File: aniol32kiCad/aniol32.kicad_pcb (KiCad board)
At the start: 2 copper layers, 55 parts, among them J1 RST, J2 PWR, J5 Buzzer, U1 74LS32, U10 74LS590, U11 74LS573, U12 74LS74, U13 74LS151, U14 74LS138, U2 74LS14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

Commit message: added bitmapped text bin file generator
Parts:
- removed U8: KM62256CLP, Package_DIP:DIP-28_W15.24mm_Socket
- CPU1: renamed from U6; value Z80CPU -> Z80
- D1: footprint Diode_THT:D_A-405_P7.62mm_Horizontal -> Diode_THT:D_5KPW_P7.62mm_Vertical_AnodeUp
- R11, R13: value 1k -> 4k7
- SERIAL1: value Conn_02x08_Counter_Clockwise -> Conn_02x08
- U9: value DART-DIP-40 -> DART
- moved R1 75.3 mm to (246.8, 135.0)
- moved R4 75.3 mm to (226.7, 124.7)
- moved R6 75.3 mm to (230.7, 114.4)
- moved R8 75.3 mm to (230.7, 118.5)
- moved RV1 75.3 mm to (219.4, 147.0)
- moved R2 75.3 mm to (247.4, 141.5)
- moved R5 75.3 mm to (215.9, 128.7)
- moved R7 75.3 mm to (215.9, 124.7)
- moved C3 66.4 mm to (125.1, 39.1), turned to 0 degrees
- moved ROM1 54.7 mm to (106.4, 46.6)
- moved U1 51.5 mm to (138.4, 101.1)
- moved C10 50.9 mm to (135.1, 99.6)
- moved J5 36.1 mm to (152.4, 38.9)
- moved C13 32.9 mm to (80.6, 57.5)
- moved U13 32.9 mm to (83.9, 58.7)
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- renumbered U7 to ROM1
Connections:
- CPU1 pad 17: Net-(R11-Pad1) -> NMI
- CPU1 pad 24: Net-(R13-Pad1) -> WAIT
- CPU1 pad 29: (no net) -> GND
- CPU1 pad 5: A15 -> (no net)
- R11 pad 1: Net-(R11-Pad1) -> NMI
- R13 pad 1: Net-(R13-Pad1) -> WAIT
- ROM1 pad 20: ROMSEL -> MEMRQ
- SERIAL1 pad 11: (no net) -> Net-(SERIAL1-Pad11)
- SERIAL1 pad 13: (no net) -> Net-(SERIAL1-Pad13)
- SERIAL1 pad 14: (no net) -> Net-(SERIAL1-Pad14)
- SERIAL1 pad 15: (no net) -> Net-(SERIAL1-Pad15)
- SERIAL1 pad 16: +5V -> GND
- SERIAL1 pad 7: Net-(SERIAL1-Pad7) -> CLK
- SERIAL1 pad 8: GND -> +5V
- SERIAL1 pad 9: CLK -> Net-(SERIAL1-Pad9)
- U1 pad 1: A15 -> (no net)
- U1 pad 2: MEMRQ -> (no net)
- U1 pad 3: RAMSEL -> (no net)
- U1 pad 4: MEMRQ -> (no net)
- U1 pad 5: Net-(U1-Pad5) -> (no net)
- U1 pad 6: ROMSEL -> (no net)
- U2 pad 1: A15 -> (no net)
- U2 pad 2: Net-(U1-Pad5) -> (no net)
- U9 pad 11: (no net) -> Net-(SERIAL1-Pad6)
- U9 pad 12: (no net) -> Net-(SERIAL1-Pad2)
- U9 pad 13: (no net) -> Net-(SERIAL1-Pad3)
- U9 pad 14: (no net) -> Net-(SERIAL1-Pad5)
- U9 pad 15: (no net) -> Net-(SERIAL1-Pad4)
- U9 pad 22: Net-(SERIAL1-Pad10) -> Net-(SERIAL1-Pad1)
- U9 pad 23: Net-(SERIAL1-Pad6) -> Net-(SERIAL1-Pad14)
- U9 pad 24: Net-(SERIAL1-Pad5) -> Net-(SERIAL1-Pad13)
- U9 pad 25: Net-(SERIAL1-Pad7) -> Net-(SERIAL1-Pad15)
- U9 pad 26: Net-(SERIAL1-Pad2) -> Net-(SERIAL1-Pad10)
- U9 pad 28: Net-(SERIAL1-Pad1) -> Net-(SERIAL1-Pad9)
- U9 pad 29: Net-(SERIAL1-Pad3) -> Net-(SERIAL1-Pad11)
- U9 pad 30: Net-(SERIAL1-Pad4) -> WAIT

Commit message: working on the calculator and the A32 pcb
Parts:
- D1: footprint Diode_THT:D_5KPW_P7.62mm_Vertical_AnodeUp -> Diode_THT:D_DO-15_P2.54mm_Vertical_AnodeUp
- RV1: footprint Potentiometer_THT:Potentiometer_TT_P0915N -> Potentiometer_THT:Potentiometer_Vishay_T73XW_Horizontal
- moved R2 251.9 mm to (14.6, 45.2)
- moved R1 201.7 mm to (72.5, 33.4), turned to 180 degrees
- moved RV1 186.9 mm to (85.9, 16.3), turned to 90 degrees
- moved R8 155.2 mm to (89.7, 53.6), turned to 90 degrees
- moved R6 147.5 mm to (96.3, 53.6), turned to 90 degrees
- moved R7 142.0 mm to (93.0, 53.6), turned to 90 degrees
- moved R5 138.5 mm to (99.6, 53.6), turned to 90 degrees
- moved R4 81.2 mm to (148.5, 102.7), turned to 90 degrees
- moved C7 40.4 mm to (110.2, 44.4)
- moved U3 40.4 mm to (113.5, 45.6)
- moved ROM1 34.0 mm to (140.3, 49.4)
- moved C3 34.0 mm to (159.0, 41.9)
- moved J5 25.3 mm to (172.3, 23.2)
- moved U4 23.9 mm to (158.4, 84.8)
- moved C2 23.3 mm to (154.9, 83.1)
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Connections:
- U12 pad 13: GND -> +5V

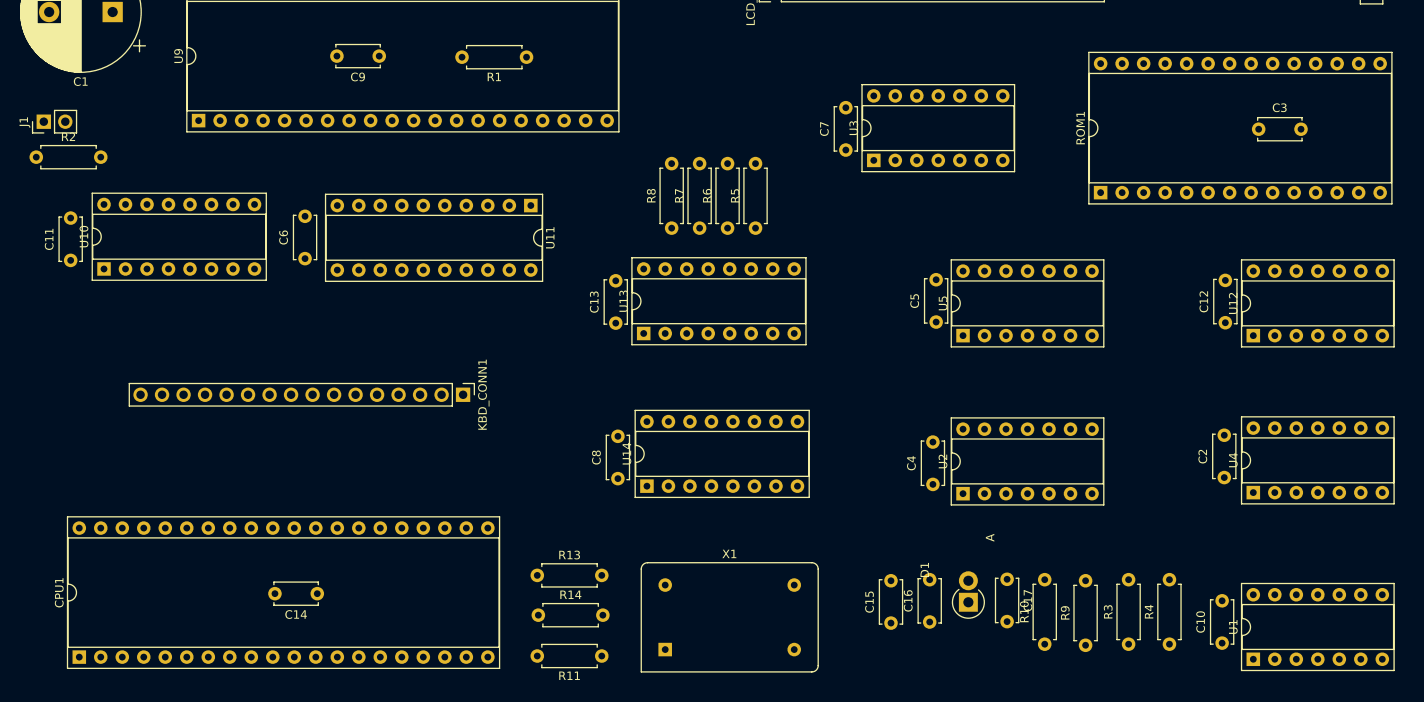
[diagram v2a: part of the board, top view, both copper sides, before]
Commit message: New A32 PCB layout
With CPU closer to the memory
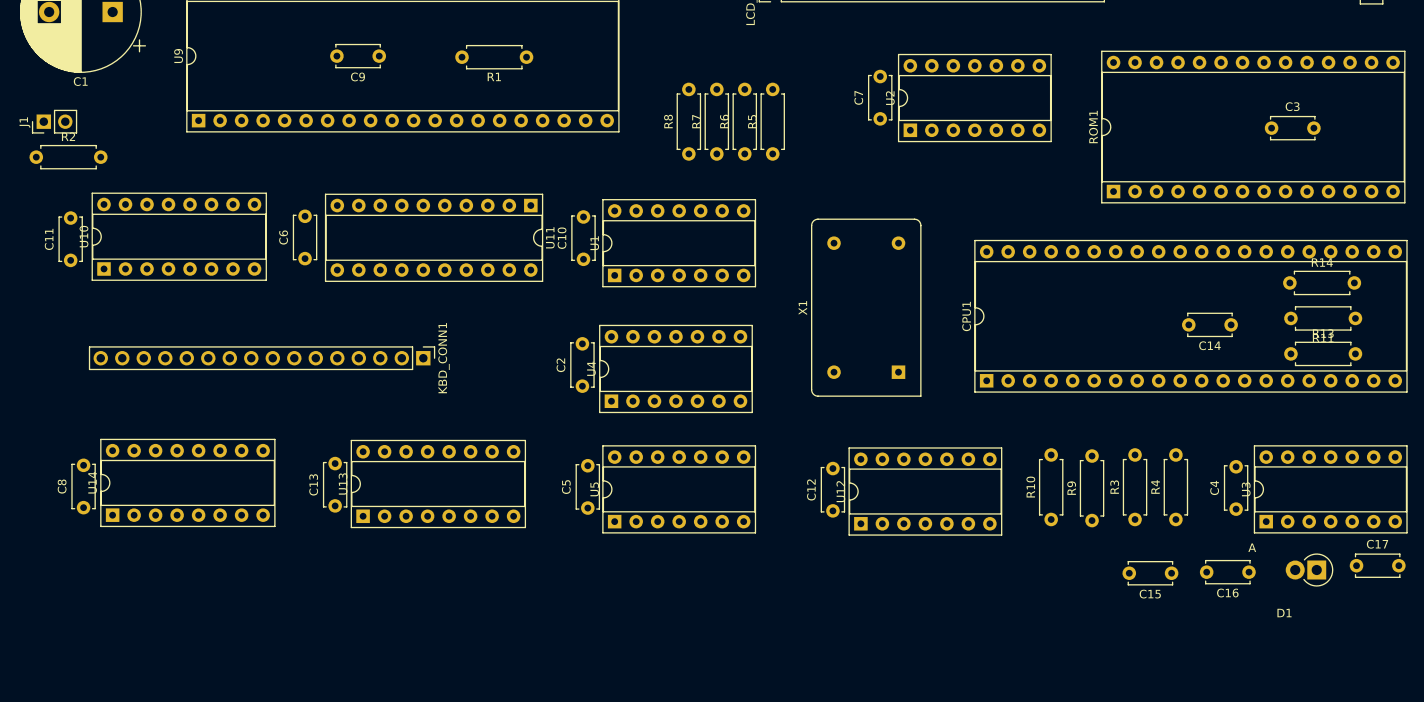
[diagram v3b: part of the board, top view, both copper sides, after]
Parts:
- moved C14 112.5 mm to (155.7, 65.0)
- moved CPU1 112.0 mm to (126.9, 71.6)
- moved R11 97.6 mm to (170.4, 64.3)
- moved R14 97.1 mm to (162.7, 60.1)
- moved R13 92.8 mm to (162.8, 68.5)
- moved C10 88.0 mm to (79.2, 57.3)
- moved U1 88.0 mm to (82.9, 59.2)
- moved C2 76.6 mm to (79.1, 72.3)
- moved U4 76.6 mm to (82.5, 74.0)
- moved C8 63.2 mm to (20.2, 86.6)
- moved U14 63.2 mm to (23.6, 87.5)
- moved U3 63.0 mm to (159.9, 88.3)
- moved C12 51.4 mm to (108.7, 87.0)
- moved U12 51.4 mm to (112.0, 88.5)
- moved C5 46.6 mm to (79.8, 86.7)
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
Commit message: tidied up the PCB
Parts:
- removed SERIAL1: Conn_02x08, Connector_PinSocket_2.54mm:PinSocket_2x08_P2.54mm_Horizontal
- added J3: Conn_02x08_Odd_Even, Connector_PinSocket_2.54mm:PinSocket_2x08_P2.54mm_Horizontal, F.Cu at (70.1, 15.5)
- D1: footprint Diode_THT:D_DO-15_P2.54mm_Vertical_AnodeUp -> Diode_THT:D_5KPW_P7.62mm_Vertical_AnodeUp
- RV1: footprint Potentiometer_THT:Potentiometer_Vishay_T73XW_Horizontal -> Potentiometer_THT:Potentiometer_TT_P0915N
- moved C15 18.7 mm to (148.8, 75.7)
- moved C16 18.7 mm to (158.0, 75.6)
- moved C17 18.7 mm to (170.7, 74.8)
- moved D1 18.7 mm to (166.0, 75.3)
- moved C1 8.52 mm to (15.1, 28.3), turned to 0 degrees
- moved LCD_CONN1 8.38 mm to (93.0, 25.5)
- moved R11 8.21 mm to (162.8, 61.2), turned to 0 degrees
- moved ROM1 6.99 mm to (141.9, 42.3)
- moved C3 6.98 mm to (160.5, 34.8)
- moved J1 6.48 mm to (22.0, 40.9), turned to 270 degrees
- moved J5 6.25 mm to (174.9, 17.5)
- moved C8 5.72 mm to (19.9, 80.9), turned to 270 degrees
- moved C11 5.09 mm to (18.9, 52.3), turned to 270 degrees
- moved RN1 5.08 mm to (105.7, 17.9)
- moved C5 5.01 mm to (79.5, 81.7), turned to 270 degrees
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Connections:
- RN1 pad 2: D7 -> D0
- RN1 pad 3: D6 -> D1
- RN1 pad 4: D5 -> D2
- RN1 pad 5: D4 -> D3
- RN1 pad 6: D3 -> D4
- RN1 pad 7: D2 -> D5
- RN1 pad 8: D1 -> D6
- RN1 pad 9: D0 -> D7

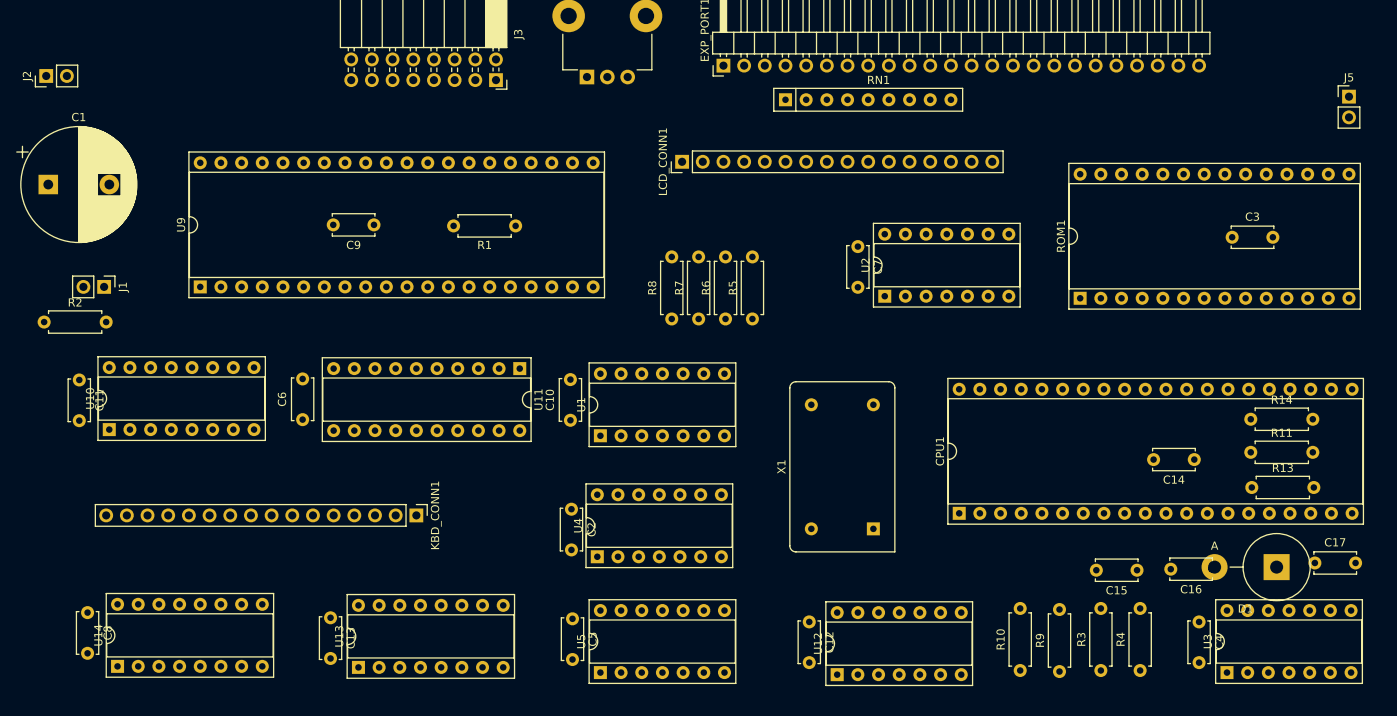
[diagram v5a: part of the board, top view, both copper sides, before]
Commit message: Doc changes
Removed a '32 from A32
Documented the VGA connector
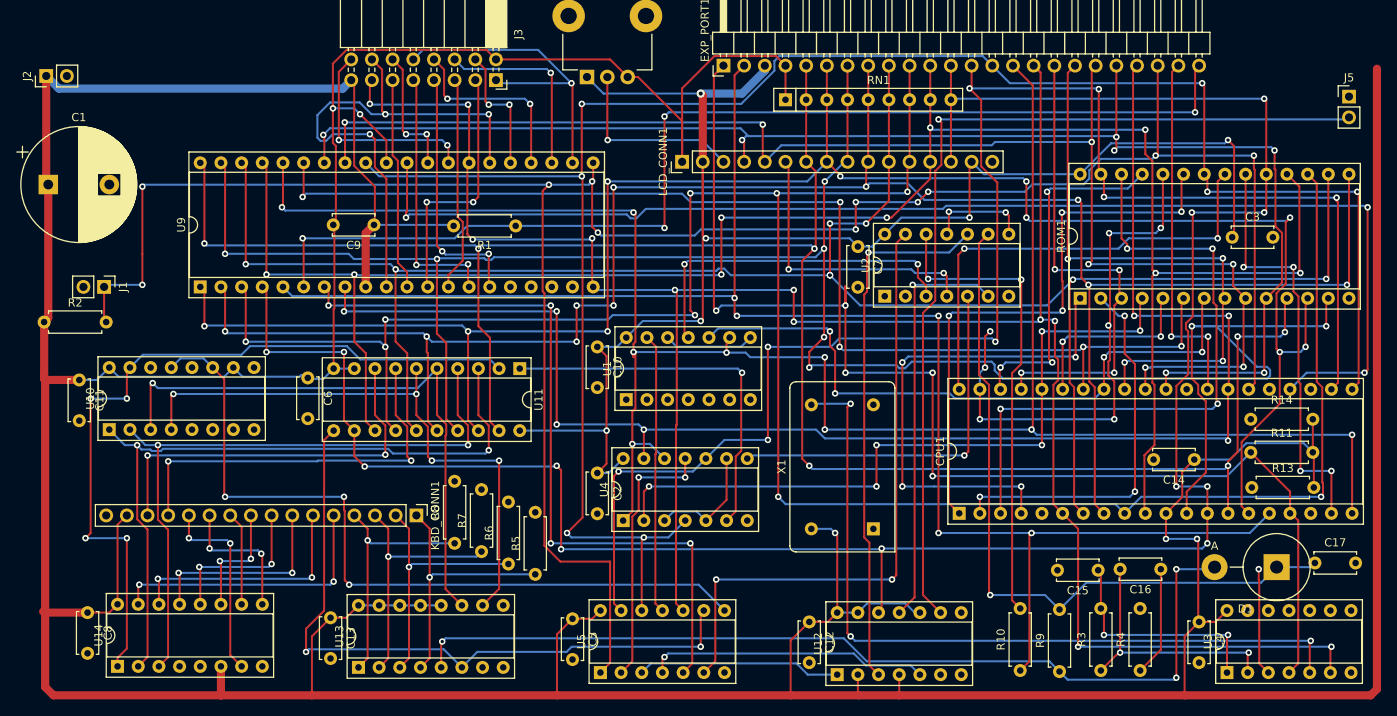
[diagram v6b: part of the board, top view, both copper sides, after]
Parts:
- moved R5 41.2 mm to (74.9, 76.2)
- moved R6 40.2 mm to (71.6, 74.9)
- moved R7 39.1 mm to (68.3, 73.4)
- moved R8 38.4 mm to (65.0, 72.4)
- moved C10 9.60 mm to (82.5, 48.3), turned to 270 degrees
- moved C16 6.22 mm to (151.8, 75.6)
- moved C2 5.46 mm to (82.5, 63.8)
- moved U1 5.46 mm to (86.1, 54.7)
- moved U4 5.46 mm to (85.7, 69.6)
- moved C6 5.17 mm to (47.0, 52.1), turned to 270 degrees
- moved C15 4.78 mm to (144.1, 75.7)
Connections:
- J3 pad 1: Net-(J3-Pad1) -> (no net)
- J3 pad 10: (no net) -> Net-(J3-Pad10)
- U9 pad 10: (no net) -> Net-(J3-Pad14)
- U9 pad 22: Net-(J3-Pad1) -> Net-(J3-Pad10)
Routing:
- net +5V: track 0.00 -> 789.5 mm, vias 0 -> 9
- net RST: track 0.00 -> 281.0 mm, vias 0 -> 11
- net D5: track 0.00 -> 280.5 mm, vias 0 -> 9
- net D7: track 0.00 -> 273.6 mm, vias 0 -> 12
- net D2: track 0.00 -> 263.3 mm, vias 0 -> 8
- net CLK: track 0.00 -> 261.2 mm, vias 0 -> 11
- net IORQ: track 0.00 -> 248.8 mm, vias 0 -> 9
- net D0: track 0.00 -> 244.3 mm, vias 0 -> 7
- net D6: track 0.00 -> 244.2 mm, vias 0 -> 9
- net D4: track 0.00 -> 243.8 mm, vias 0 -> 8
- net D3: track 0.00 -> 243.3 mm, vias 0 -> 10
- net RD: track 0.00 -> 242.8 mm, vias 0 -> 7
- net D1: track 0.00 -> 237.5 mm, vias 0 -> 10
- net INT: track 0.00 -> 197.9 mm, vias 0 -> 5
- net WR: track 0.00 -> 195.1 mm, vias 0 -> 8
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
